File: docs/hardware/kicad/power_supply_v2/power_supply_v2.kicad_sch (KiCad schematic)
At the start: 109 parts, among them J1 Barrel_Jack, J2 LOAD 3V3, J3 LOAD 5V, J4 LOAD Vvar, M1 Fan_4pin, U1 TPS54302, U10 NUCLEO-G474RE, U11 INA180A3, U12 INA180A3, U13 INA180A1, U14 SHT31-DIS, U15 SHT31-DIS, U2 MCP1700T, U3 TPS22917DBV, U4 TPS54302, U5 MCP1700T, U6 SN74AHCT125N, U7 TPS22917DBV, U8 TPS54302, U9 TPS54302

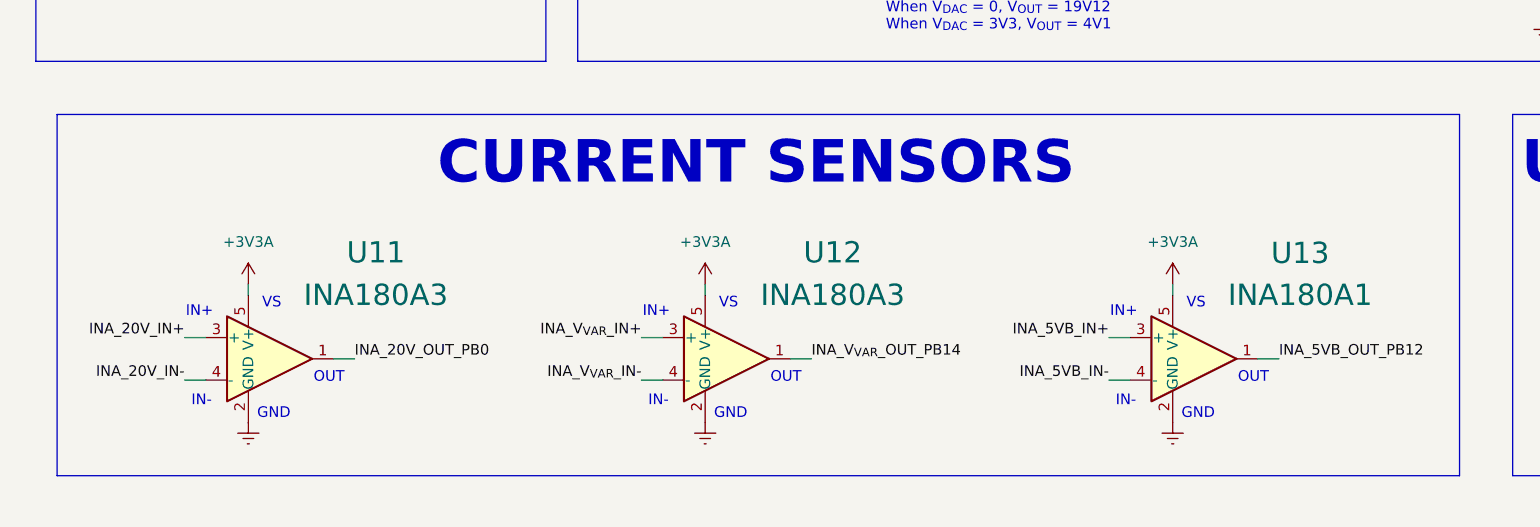
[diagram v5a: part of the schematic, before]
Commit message: add mising bypass caps to INAs in schematic
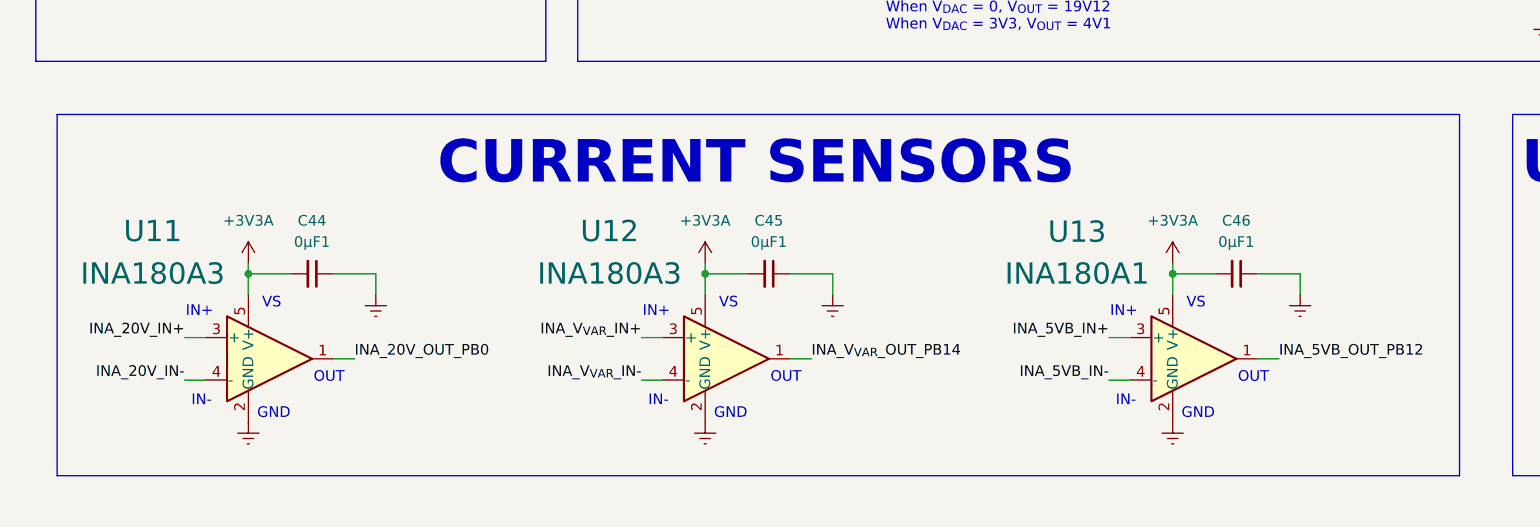
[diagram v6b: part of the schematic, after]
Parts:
- added C44, C45, C46: 0μF1, symbol Library:C_Small
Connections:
- net +3V3A: now also C44.2, C45.2, C46.2
- net GNDREF: now also C44.1, C45.1, C46.1

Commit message: add RC filter to INA outs and fix divider equation resistor variables
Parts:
- added C47, C48, C49: 10nF, symbol Library:C_Small
- added R28, R29, R30: 100R, symbol Library:R_Small_US
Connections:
- net GNDREF: now also C47.1, C48.1, C49.1
- net INA_20V_OUT_PB0: now also C47.2, R28.2; no longer U11.1
- net INA_5VB_OUT_PB12: now also C49.2, R30.2; no longer U13.1
- net INA_V_{VAR}_OUT_PB14: now also C48.2, R29.2; no longer U12.1
- new net: R30.1, U13.1
- new net: R29.1, U12.1
- new net: R28.1, U11.1
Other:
- note added: "V_{OUT} = 0.596 * (1 + R19 / (R20 + R21)) V_{OUT} = 12V12"
- note added: "V_{OUT} = 0.596 * (1 + R23 / (R24 + R25)) + R23 / R26) - V_{DAC} * (R23 / R26) V_{DAC} = 0 to 3V3 R23 / (R24 + R25) = 26R53 R23 / R26 = 4R55 When V_{DAC} = 0, V_{OUT} = 19V12 When V_{DAC} = 3V3, V_{OUT} = 4V1"
- note added: "V_{OUT} = 0.596 * (1 + R9 / R10 + R9 / R11) - V_{DAC} * (R9 / R11) V_{DAC} = 0 to 3V3 R9 / R10 = 6R67 R9 / R11 = 2R13 When V_{DAC} = 0, V_{OUT} = 5V84 When V_{DAC} = 3V3, V_{OUT} = -1V19"
- note removed: "V_{out} = 0.596 * (1 + R15 / (R16 + R17) + R15 / R18) - V_{DAC} * (R15 / R18) V_{DAC} = 0 to 3V3 R15 / (R16 + R17) = 26R53 R15 / R18 = 4R55 When V_{DAC} = 0, V_{OUT} = 19V12 When V_{DAC} = 3V3, V_{OUT} = 4V1"
- note removed: "V_{out} = 0.596 * (1 + R7 / R8 + R7 / R9) - V_{DAC} * (R7 / R9) V_{DAC} = 0 to 3V3 R7 / R8 = 2R13 R7 / R9 = 6R67 When V_{DAC} = 0, V_{OUT} = 5V84 When V_{DAC} = 3V3, V_{OUT} = -1V19"
- moved on the sheet: C44, C45, C46, S1, S2, U11, U12, U13, U14, U15
